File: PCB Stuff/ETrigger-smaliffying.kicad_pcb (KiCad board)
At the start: 2 copper layers, 33.7 x 27.5 mm, 53 parts, among them IC1 ATTINY85-S, P1 CONN_01X04, Q1 S8550, Q2 S8550, U1 AP1117, U4 LM321C

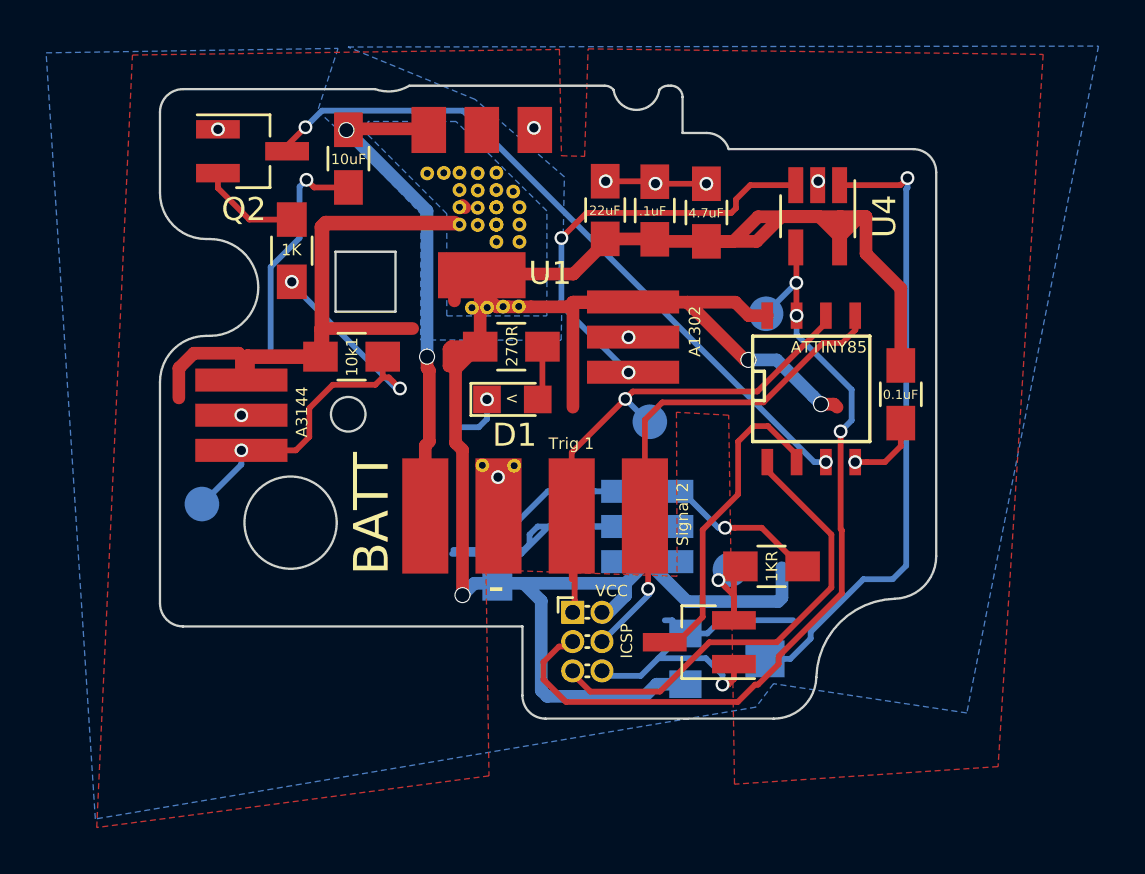
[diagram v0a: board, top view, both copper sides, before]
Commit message: Small Changes Already...
THe VReg didnt have mask clearance in the footprint and I didnt notice
it because the pads werent covered in the 3d viewer, good thing there is
gerber viewers...
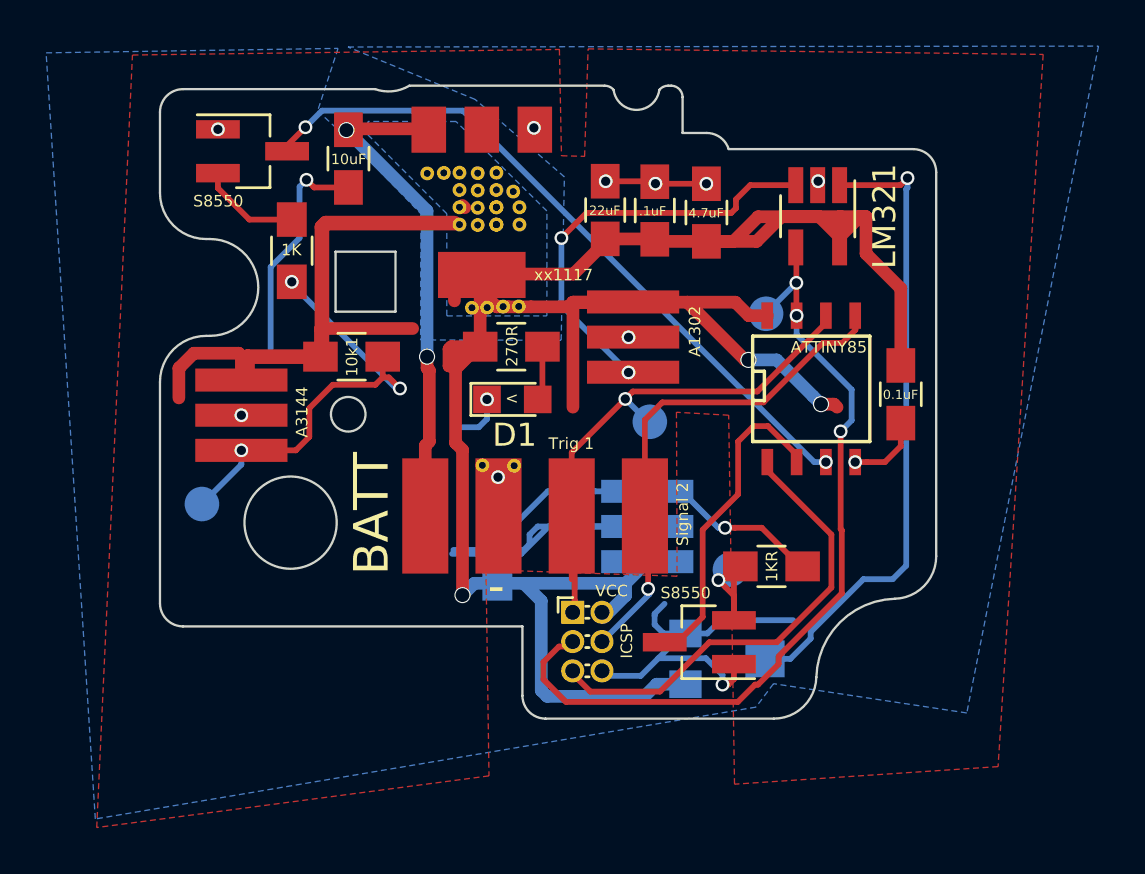
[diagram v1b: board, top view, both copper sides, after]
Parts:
- removed the REF** at (152.5, 90.8)
- removed the REF** at (151.5, 90.8)
- renumbered U4 to LM321, Q1 to S8550, Q2 to S8550, U1 to xx1117
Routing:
- net VCC_ICSP: track 140.6 -> 132.7 mm
- net GND_ICSP: track 56.4 -> 57.8 mm
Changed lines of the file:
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@@
 (kicad_pcb (version 4) (host pcbnew 4.0.5)
   (general
-    (links 82)
+    (links 0)
     (no_connects 0)
     (area 136.830709 82.456999 170.595002 111.507001)
     (thickness 1.6)
     (drawings 248)
-    (tracks 319)
+    (tracks 318)
     (zones 0)
-    (modules 53)
+    (modules 51)
     (nets 17)
   )
   (page A4)
   (layers
-    (0 F.Cu signal)
+    (0 F.Cu signal hide)
     (31 B.Cu signal)
     (32 B.Adhes user)
@@
     (visible_elements 7FFEF6FF)
     (pcbplotparams
-      (layerselection 0x00030_80000001)
-      (usegerberextensions false)
+      (layerselection 0x011f0_80000001)
+      (usegerberextensions true)
       (excludeedgelayer true)
       (linewidth 0.100000)
@@
       (outputformat 1)
       (mirror false)
-      (drillshape 1)
+      (drillshape 0)
       (scaleselection 1)
-      (outputdirectory ""))
+      (outputdirectory "ETrig Board/"))
   )
   (net 0 "")
@@
     (add_net VCC_ICSP)
   )
+  (module TO_SOT_Packages_SMD:SOT-223 (layer F.Cu)
+    (at 150.8379 89.0647 270)
+    (descr "module CMS SOT223 4 pins")
+    (tags "CMS SOT")
+    (attr smd)
+    (fp_text reference xx1117 (at 3.15 -3.5433 360) (layer F.SilkS)
+      (effects (font (size 0.5 0.5) (thickness 0.1)))
+    )
+    (fp_text value AP1117 (at 0 4.5 270) (layer F.Fab)
+      (effects (font (size 1 1) (thickness 0.15)))
+    )
+    (fp_text user %R (at 0 0 270) (layer F.Fab)
+      (effects (font (size 0.8 0.8) (thickness 0.12)))
+    )
+    (fp_line (start -1.85 -2.3) (end -0.8 -3.35) (layer F.Fab) (width 0.1))
+    (fp_line (start 4.4 -3.6) (end -4.4 -3.6) (layer F.CrtYd) (width 0.05))
+    (fp_line (start 4.4 3.6) (end 4.4 -3.6) (layer F.CrtYd) (width 0.05))
+    (fp_line (start -4.4 3.6) (end 4.4 3.6) (layer F.CrtYd) (width 0.05))
+    (fp_line (start -4.4 -3.6) (end -4.4 3.6) (layer F.CrtYd) (width 0.05))
+    (fp_line (start -1.85 -2.3) (end -1.85 3.35) (layer F.Fab) (width 0.1))
+    (fp_line (start -0.8 -3.35) (end 1.85 -3.35) (layer F.Fab) (width 0.1))
+    (fp_line (start -1.85 3.35) (end 1.85 3.35) (layer F.Fab) (width 0.1))
+    (fp_line (start 1.85 -3.35) (end 1.85 3.35) (layer F.Fab) (width 0.1))
+    (pad 4 smd rect (at 3.15 0 270) (size 2 3.8) (layers *.Mask F.Cu F.Paste)
+      (net 1 VCC_ICSP) (zone_connect 2))
+    (pad 2 smd rect (at -3.15 0 270) (size 2 1.5) (layers *.Mask F.Cu F.Paste)
+      (net 1 VCC_ICSP))
+    (pad 3 smd rect (at -3.15 2.3 270) (size 2 1.5) (layers *.Mask F.Cu F.Paste)
+      (net 4 +BATT))
+    (pad 1 smd rect (at -3.15 -2.3 270) (size 2 1.5) (layers *.Mask F.Cu F.Paste)
+      (net 5 GND_ICSP))
+    (model ${KISYS3DMOD}/TO_SOT_Packages_SMD.3dshapes/SOT-223.wrl
+      (at (xyz 0 0 0))
+      (scale (xyz 0.5 0.5 0.5))
+      (rotate (xyz 0 0 90))
+    )
+  )
   (module Capacitors_SMD:C_0805_HandSoldering (layer F.Cu)
     (at 169.01 97.39 270)
@@
   )
   (module "Via 2" (layer F.Cu)
-    (at 152.47 90.78)
-    (clearance 0.00001)
-    (zone_connect 2)
-    (fp_text reference REF** (at 0.127 4.699) (layer F.SilkS) hide
-      (effects (font (size 0.127 0.127) (thickness 0.03175)))
-    )
-    (fp_text value "Via 2" (at -0.127 -5.969) (layer F.Fab) hide
-      (effects (font (size 0.127 0.127) (thickness 0.03175)))
-    )
-    (pad 1 thru_hole circle (at 0 0) (size 0.6 0.6) (drill 0.3) (layers *.Cu)
-      (net 1 VCC_ICSP) (zone_connect 2))
-  )
-  (module "Via 2" (layer F.Cu)
-    (at 151.47 90.78)
-    (clearance 0.00001)
-    (zone_connect 2)
-    (fp_text reference REF** (at 0.127 4.699) (layer F.SilkS) hide
-      (effects (font (size 0.127 0.127) (thickness 0.03175)))
-    )
-    (fp_text value "Via 2" (at -0.127 -5.969) (layer F.Fab) hide
-      (effects (font (size 0.127 0.127) (thickness 0.03175)))
-    )
-    (pad 1 thru_hole circle (at 0 0) (size 0.6 0.6) (drill 0.3) (layers *.Cu)
-      (net 1 VCC_ICSP) (zone_connect 2))
-  )
-  (module "Via 2" (layer F.Cu)
     (at 152.47 90.03)
     (clearance 0.00001)
@@
     (pad 1 thru_hole circle (at 0 0) (size 0.6 0.6) (drill 0.3) (layers *.Cu)
       (net 5 GND_ICSP) (zone_connect 2))
-  )
-  (module TO_SOT_Packages_SMD:SOT-223 (layer F.Cu)
-    (at 150.8379 89.0774 270)
-    (descr "module CMS SOT223 4 pins")
-    (tags "CMS SOT")
-    (attr smd)
-    (fp_text reference U1 (at 3.0611 -2.9591 360) (layer F.SilkS)
-      (effects (font (size 1 1) (thickness 0.15)))
-    )
-    (fp_text value AP1117 (at 0 4.5 270) (layer F.Fab)
-      (effects (font (size 1 1) (thickness 0.15)))
-    )
-    (fp_text user %R (at 0 0 270) (layer F.Fab)
-      (effects (font (size 0.8 0.8) (thickness 0.12)))
-    )
-    (fp_line (start -1.85 -2.3) (end -0.8 -3.35) (layer F.Fab) (width 0.1))
-    (fp_line (start 4.4 -3.6) (end -4.4 -3.6) (layer F.CrtYd) (width 0.05))
-    (fp_line (start 4.4 3.6) (end 4.4 -3.6) (layer F.CrtYd) (width 0.05))
-    (fp_line (start -4.4 3.6) (end 4.4 3.6) (layer F.CrtYd) (width 0.05))
-    (fp_line (start -4.4 -3.6) (end -4.4 3.6) (layer F.CrtYd) (width 0.05))
-    (fp_line (start -1.85 -2.3) (end -1.85 3.35) (layer F.Fab) (width 0.1))
-    (fp_line (start -0.8 -3.35) (end 1.85 -3.35) (layer F.Fab) (width 0.1))
-    (fp_line (start -1.85 3.35) (end 1.85 3.35) (layer F.Fab) (width 0.1))
-    (fp_line (start 1.85 -3.35) (end 1.85 3.35) (layer F.Fab) (width 0.1))
-    (pad 4 smd rect (at 3.15 0 270) (size 2 3.8) (layers F.Cu F.Paste)
-      (net 1 VCC_ICSP) (zone_connect 2))
-    (pad 2 smd rect (at -3.15 0 270) (size 2 1.5) (layers F.Cu F.Paste)
-      (net 1 VCC_ICSP))
-    (pad 3 smd rect (at -3.15 2.3 270) (size 2 1.5) (layers F.Cu F.Paste)
-      (net 4 +BATT))
-    (pad 1 smd rect (at -3.15 -2.3 270) (size 2 1.5) (layers F.Cu F.Paste)
-      (net 5 GND_ICSP))
-    (model ${KISYS3DMOD}/TO_SOT_Packages_SMD.3dshapes/SOT-223.wrl
-      (at (xyz 0 0 0))
-      (scale (xyz 0.5 0.5 0.5))
-      (rotate (xyz 0 0 90))
-    )
   )
   (module Via (layer F.Cu)
@@
     (tags "SOT-23-5 hand-soldering")
     (attr smd)
-    (fp_text reference U4 (at 0 -2.9 270) (layer F.SilkS)
+    (fp_text reference LM321 (at 0 -2.9 270) (layer F.SilkS)
       (effects (font (size 1 1) (thickness 0.15)))
     )
@@
     (tags SOT-23)
     (attr smd)
-    (fp_text reference Q1 (at 0 -2.5 180) (layer F.SilkS) hide
-      (effects (font (size 1 1) (thickness 0.15)))
+    (fp_text reference S8550 (at 0.5955 2.13614 180) (layer F.SilkS)
+      (effects (font (size 0.5 0.5) (thickness 0.1)))
     )
     (fp_text value S8550 (at 0 2.5 180) (layer F.Fab)
@@
       (at (xyz 0 0 0))
       (scale (xyz 1 1 1))
-      (rotate (xyz 0 0 0))
+      (rotate (xyz 0 0 90))
     )
   )
@@
     (tags SOT-23)
     (attr smd)
-    (fp_text reference Q2 (at -0.3738 2.51978) (layer F.SilkS)
-      (effects (font (size 1 1) (thickness 0.15)))
+    (fp_text reference S8550 (at -1.4859 2.16408) (layer F.SilkS)
+      (effects (font (size 0.5 0.5) (thickness 0.1)))
     )
     (fp_text value S8550 (at 0 2.5) (layer F.Fab)
@@
       (at (xyz 0 0 0))
       (scale (xyz 1 1 1))
-      (rotate (xyz 0 0 0))
+      (rotate (xyz 0 0 90))
     )
   )
@@
     (tags "Mesurement Point Round SMD Pad 1.5mm")
     (attr virtual)
-    (fp_text reference W4 (at 0.04 -2.78) (layer B.SilkS)
+    (fp_text reference W4 (at 0.1091 -1.7617) (layer B.SilkS)
       (effects (font (size 1 1) (thickness 0.15)) (justify mirror))
     )
@@
   (via (at 162.4 95.9) (size 0.7) (drill 0.6) (layers F.Cu B.Cu) (net 1))
   (segment (start 162.2548 95.9) (end 162.4 95.9) (width 0.55) (layer F.Cu) (net 1))
-  (segment (start 159.745317 106.379917) (end 158.0134 104.648) (width 0.55) (layer B.Cu) (net 1))
-  (segment (start 163.688283 106.379917) (end 159.745317 106.379917) (width 0.55) (layer B.Cu) (net 1))
-  (segment (start 163.8554 106.2128) (end 163.688283 106.379917) (width 0.55) (layer B.Cu) (net 1))
-  (segment (start 163.8554 104.9128) (end 163.8554 106.2128) (width 0.55) (layer B.Cu) (net 1))
   (segment (start 137.7 96.26) (end 137.7 97.55) (width 0.55) (layer F.Cu) (net 1))
   (segment (start 137.74 96.22) (end 137.7 96.26) (width 0.55) (layer F.Cu) (net 1))
@@
   (via (at 144.966145 85.934137) (size 0.7) (drill 0.6) (layers F.Cu B.Cu) (net 4))
   (via (at 148.463 95.758) (size 0.7) (drill 0.6) (layers F.Cu B.Cu) (net 4))
+  (segment (start 158.3309 106.9086) (end 158.7627 106.4768) (width 0.25) (layer B.Cu) (net 5))
+  (segment (start 158.3309 106.9975) (end 158.3309 106.9086) (width 0.25) (layer B.Cu) (net 5))
+  (segment (start 158.3309 107.3765) (end 158.3309 106.9975) (width 0.25) (layer B.Cu) (net 5))
+  (segment (start 159.6688 107.7644) (end 158.7188 107.7644) (width 0.25) (layer B.Cu) (net 5))
+  (segment (start 158.7188 107.7644) (end 158.3309 107.3765) (width 0.25) (layer B.Cu) (net 5))
   (segment (start 152.673615 85.835353) (end 153.097879 85.835353) (width 0.25) (layer F.Cu) (net 5))
   (segment (start 152.654847 85.835353) (end 152.673615 85.835353) (width 0.25) (layer F.Cu) (net 5))
@@
   (segment (start 151.5618 102.6668) (end 151.541135 102.646135) (width 0.25) (layer F.Cu) (net 5))
   (via (at 151.541135 100.983493) (size 0.6) (drill 0.4) (layers F.Cu B.Cu) (net 5))
-  (segment (start 158.7726 107.19304) (end 159.09744 107.19304) (width 0.25) (layer B.Cu) (net 5))
-  (segment (start 159.09744 107.19304) (end 159.6688 107.7644) (width 0.25) (layer B.Cu) (net 5))
   (via (at 139.3938 85.90022) (size 0.6) (drill 0.4) (layers F.Cu B.Cu) (net 5))
   (via (at 151.0636 97.6122) (size 0.6) (drill 0.4) (layers F.Cu B.Cu) (net 5))
@@
       )
     )
-  )
-  (zone (net 0) (net_name "") (layer F.Mask) (hatch edge 0.508)
-    (connect_pads (clearance 0.508))
-    (min_thickness 0.254)
-    (fill yes (arc_segments 16) (thermal_gap 0.508) (thermal_bridge_width 0.508))
-    (polygon
-      (pts
-        (xy 147.32 91.059) (xy 147.32 87.122) (xy 154.305 87.122) (xy 154.305 91.059)
-      )
-    )
